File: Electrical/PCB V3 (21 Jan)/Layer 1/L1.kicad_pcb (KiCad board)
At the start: 2 copper layers, 178 x 170 mm, 198 parts, among them J1 Conn_01x02, J3 Conn_01x02, SW1 SW_SPDT, U2 CD74HC4067SM, U3 CD74HC4067SM, U4 XT30UPB-M, U5 113991054

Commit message: finished l1?
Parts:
- J1, J3, TP1: footprint Connector_PinHeader_1.00mm:PinHeader_1x02_P1.00mm_Vertical -> Connector_PinHeader_2.54mm:PinHeader_1x02_P2.54mm_Vertical
- R33, R34: footprint Resistor_SMD:R_0201_0603Metric -> Resistor_SMD:R_0603_1608Metric
- moved U4 245.9 mm to (83.2, 35.6), turned to -45 degrees
- moved U5 196.2 mm to (113.8, 37.8)
- moved SW1 180.9 mm to (89.1, 32.3), turned to 45 degrees
- moved TP1 174.7 mm to (97.7, 37.0), turned to 180 degrees
- moved J3 167.2 mm to (102.2, 36.8), turned to 180 degrees
- moved R33 163.9 mm to (109.0, 29.4), turned to -90 degrees
- moved R34 162.8 mm to (109.1, 33.7), turned to 90 degrees
- moved J1 162.2 mm to (102.2, 43.1), turned to 180 degrees
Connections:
- L10 pad 1: Net-(LED1-A) -> Net-(LED10-A)
- L10 pad 2: Net-(L1-Pad2) -> Net-(L10-Pad2)
- L11 pad 1: Net-(LED1-A) -> Net-(LED11-A)
- L11 pad 2: Net-(L1-Pad2) -> Net-(L11-Pad2)
- L12 pad 1: Net-(LED1-A) -> Net-(LED12-A)
- L12 pad 2: Net-(L1-Pad2) -> Net-(L12-Pad2)
- L13 pad 1: Net-(LED1-A) -> Net-(LED13-A)
- L13 pad 2: Net-(L1-Pad2) -> Net-(L13-Pad2)
- L14 pad 1: Net-(LED1-A) -> Net-(LED14-A)
- L14 pad 2: Net-(L1-Pad2) -> Net-(L14-Pad2)
- L15 pad 1: Net-(LED1-A) -> Net-(LED15-A)
- L15 pad 2: Net-(L1-Pad2) -> Net-(L15-Pad2)
- L16 pad 1: Net-(LED1-A) -> Net-(LED16-A)
- L16 pad 2: Net-(L1-Pad2) -> Net-(L16-Pad2)
- L17 pad 1: Net-(LED1-A) -> Net-(LED17-A)
- L17 pad 2: Net-(L1-Pad2) -> Net-(L17-Pad2)
- L18 pad 1: Net-(LED1-A) -> Net-(LED18-A)
- L18 pad 2: Net-(L1-Pad2) -> Net-(L18-Pad2)
- L19 pad 1: Net-(LED1-A) -> Net-(LED19-A)
- L19 pad 2: Net-(L1-Pad2) -> Net-(L19-Pad2)
- L2 pad 1: Net-(LED1-A) -> Net-(LED2-A)
- L2 pad 2: Net-(L1-Pad2) -> Net-(L2-Pad2)
- L20 pad 1: Net-(LED1-A) -> Net-(LED20-A)
- L20 pad 2: Net-(L1-Pad2) -> Net-(L20-Pad2)
- L21 pad 1: Net-(LED1-A) -> Net-(LED21-A)
- L21 pad 2: Net-(L1-Pad2) -> Net-(L21-Pad2)
- L22 pad 1: Net-(LED1-A) -> Net-(LED22-A)
- L22 pad 2: Net-(L1-Pad2) -> Net-(L22-Pad2)
- L23 pad 1: Net-(LED1-A) -> Net-(LED23-A)
- L23 pad 2: Net-(L1-Pad2) -> Net-(L23-Pad2)
- L24 pad 1: Net-(LED1-A) -> Net-(LED24-A)
- L24 pad 2: Net-(L1-Pad2) -> Net-(L24-Pad2)
- L25 pad 1: Net-(LED1-A) -> Net-(LED25-A)
- L25 pad 2: Net-(L1-Pad2) -> Net-(L25-Pad2)
- L26 pad 1: Net-(LED1-A) -> Net-(LED26-A)
- L26 pad 2: Net-(L1-Pad2) -> Net-(L26-Pad2)
- L27 pad 1: Net-(LED1-A) -> Net-(LED27-A)
- L27 pad 2: Net-(L1-Pad2) -> Net-(L27-Pad2)
- L28 pad 1: Net-(LED1-A) -> Net-(LED28-A)
- L28 pad 2: Net-(L1-Pad2) -> Net-(L28-Pad2)
- L29 pad 1: Net-(LED1-A) -> Net-(LED29-A)
- L29 pad 2: Net-(L1-Pad2) -> Net-(L29-Pad2)
- L3 pad 1: Net-(LED1-A) -> Net-(LED3-A)
- L3 pad 2: Net-(L1-Pad2) -> Net-(L3-Pad2)
- L30 pad 1: Net-(LED1-A) -> Net-(LED30-A)
- L30 pad 2: Net-(L1-Pad2) -> Net-(L30-Pad2)
- L31 pad 1: Net-(LED1-A) -> Net-(LED31-A)
- L31 pad 2: Net-(L1-Pad2) -> Net-(L31-Pad2)
- L32 pad 1: Net-(LED1-A) -> Net-(LED32-A)
- L32 pad 2: Net-(L1-Pad2) -> Net-(L32-Pad2)
- L4 pad 1: Net-(LED1-A) -> Net-(LED4-A)
- L4 pad 2: Net-(L1-Pad2) -> Net-(L4-Pad2)
- L5 pad 1: Net-(LED1-A) -> Net-(LED5-A)
- L5 pad 2: Net-(L1-Pad2) -> Net-(L5-Pad2)
- L6 pad 1: Net-(LED1-A) -> Net-(LED6-A)
- L6 pad 2: Net-(L1-Pad2) -> Net-(L6-Pad2)
- L7 pad 1: Net-(LED1-A) -> Net-(LED7-A)
- L7 pad 2: Net-(L1-Pad2) -> Net-(L7-Pad2)
- L8 pad 1: Net-(LED1-A) -> Net-(LED8-A)
- L8 pad 2: Net-(L1-Pad2) -> Net-(L8-Pad2)
- L9 pad 1: Net-(LED1-A) -> Net-(LED9-A)
- L9 pad 2: Net-(L1-Pad2) -> Net-(L9-Pad2)
- LED10 pad 2: Net-(LED1-A) -> Net-(LED10-A)
- LED11 pad 2: Net-(LED1-A) -> Net-(LED11-A)
- LED12 pad 2: Net-(LED1-A) -> Net-(LED12-A)
- LED13 pad 2: Net-(LED1-A) -> Net-(LED13-A)
- LED14 pad 2: Net-(LED1-A) -> Net-(LED14-A)
- LED15 pad 2: Net-(LED1-A) -> Net-(LED15-A)
- LED16 pad 2: Net-(LED1-A) -> Net-(LED16-A)
- LED17 pad 2: Net-(LED1-A) -> Net-(LED17-A)
- LED18 pad 2: Net-(LED1-A) -> Net-(LED18-A)
- LED19 pad 2: Net-(LED1-A) -> Net-(LED19-A)
- LED2 pad 2: Net-(LED1-A) -> Net-(LED2-A)
- LED20 pad 2: Net-(LED1-A) -> Net-(LED20-A)
- LED21 pad 2: Net-(LED1-A) -> Net-(LED21-A)
- LED22 pad 2: Net-(LED1-A) -> Net-(LED22-A)
- LED23 pad 2: Net-(LED1-A) -> Net-(LED23-A)
- LED24 pad 2: Net-(LED1-A) -> Net-(LED24-A)
- LED25 pad 2: Net-(LED1-A) -> Net-(LED25-A)
- LED26 pad 2: Net-(LED1-A) -> Net-(LED26-A)
- LED27 pad 2: Net-(LED1-A) -> Net-(LED27-A)
- LED28 pad 2: Net-(LED1-A) -> Net-(LED28-A)
- LED29 pad 2: Net-(LED1-A) -> Net-(LED29-A)
- LED3 pad 2: Net-(LED1-A) -> Net-(LED3-A)
- LED30 pad 2: Net-(LED1-A) -> Net-(LED30-A)
- LED31 pad 2: Net-(LED1-A) -> Net-(LED31-A)
- LED32 pad 2: Net-(LED1-A) -> Net-(LED32-A)
- LED4 pad 2: Net-(LED1-A) -> Net-(LED4-A)
- LED5 pad 2: Net-(LED1-A) -> Net-(LED5-A)
- LED6 pad 2: Net-(LED1-A) -> Net-(LED6-A)
- LED7 pad 2: Net-(LED1-A) -> Net-(LED7-A)
- LED8 pad 2: Net-(LED1-A) -> Net-(LED8-A)
- LED9 pad 2: Net-(LED1-A) -> Net-(LED9-A)
- R10 pad 2: Net-(L1-Pad2) -> Net-(L10-Pad2)
- R11 pad 2: Net-(L1-Pad2) -> Net-(L11-Pad2)
- R12 pad 2: Net-(L1-Pad2) -> Net-(L12-Pad2)
- R13 pad 2: Net-(L1-Pad2) -> Net-(L13-Pad2)
- R14 pad 2: Net-(L1-Pad2) -> Net-(L14-Pad2)
- R15 pad 2: Net-(L1-Pad2) -> Net-(L15-Pad2)
- R16 pad 2: Net-(L1-Pad2) -> Net-(L16-Pad2)
- R17 pad 2: Net-(L1-Pad2) -> Net-(L17-Pad2)
- R18 pad 2: Net-(L1-Pad2) -> Net-(L18-Pad2)
- R19 pad 2: Net-(L1-Pad2) -> Net-(L19-Pad2)
- R2 pad 2: Net-(L1-Pad2) -> Net-(L2-Pad2)
- R20 pad 2: Net-(L1-Pad2) -> Net-(L20-Pad2)
- R21 pad 2: Net-(L1-Pad2) -> Net-(L21-Pad2)
- R22 pad 2: Net-(L1-Pad2) -> Net-(L22-Pad2)
- R23 pad 2: Net-(L1-Pad2) -> Net-(L23-Pad2)
- R24 pad 2: Net-(L1-Pad2) -> Net-(L24-Pad2)
- R25 pad 2: Net-(L1-Pad2) -> Net-(L25-Pad2)
- R26 pad 2: Net-(L1-Pad2) -> Net-(L26-Pad2)
- R27 pad 2: Net-(L1-Pad2) -> Net-(L27-Pad2)
- R28 pad 2: Net-(L1-Pad2) -> Net-(L28-Pad2)
- R29 pad 2: Net-(L1-Pad2) -> Net-(L29-Pad2)
- R3 pad 2: Net-(L1-Pad2) -> Net-(L3-Pad2)
- R30 pad 2: Net-(L1-Pad2) -> Net-(L30-Pad2)
- R31 pad 2: Net-(L1-Pad2) -> Net-(L31-Pad2)
- R32 pad 2: Net-(L1-Pad2) -> Net-(L32-Pad2)
- R33 pad 2: /Mux Com (1-16) -> /Mux Com (17-32)
- R34 pad 2: /Mux Com (17-32) -> /Mux Com (1-16)
- R4 pad 2: Net-(L1-Pad2) -> Net-(L4-Pad2)
- R5 pad 2: Net-(L1-Pad2) -> Net-(L5-Pad2)
- R6 pad 2: Net-(L1-Pad2) -> Net-(L6-Pad2)
- R7 pad 2: Net-(L1-Pad2) -> Net-(L7-Pad2)
- R8 pad 2: Net-(L1-Pad2) -> Net-(L8-Pad2)
- R9 pad 2: Net-(L1-Pad2) -> Net-(L9-Pad2)
- U2 pad 1: /Mux Com (1-16) -> /Mux Com (17-32)
- U3 pad 1: /Mux Com (17-32) -> /Mux Com (1-16)
- U5 pad 1: /Mux Com (1-16) -> /Mux Com (17-32)
- U5 pad 2: /Mux Com (17-32) -> /Mux Com (1-16)
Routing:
- net +3V3: track 0.00 -> 142.5 mm
- net /Mux Com (17-32): track 0.00 -> 95.9 mm, vias 0 -> 1
- net /Mux Com (1-16): track 0.00 -> 92.1 mm, vias 0 -> 1
- net /S0: track 0.00 -> 89.8 mm, vias 0 -> 3
- net /S2: track 0.00 -> 84.4 mm, vias 0 -> 3
- net /S1: track 0.00 -> 84.2 mm, vias 0 -> 3
- net /S3: track 0.00 -> 79.3 mm, vias 0 -> 3
- net Net-(LED1-A): track 72.5 -> 2.27 mm
- net Net-(L1-Pad2): track 61.2 -> 1.91 mm
- net Net-(U2-I5): track 0.00 -> 57.1 mm
- net Net-(U2-I4): track 0.00 -> 55.5 mm
- net Net-(U2-I3): track 0.00 -> 54.8 mm
- net Net-(U2-I0): track 0.00 -> 50.8 mm
- net Net-(U2-I12): track 0.00 -> 50.6 mm
- net Net-(U2-I6): track 0.00 -> 50.3 mm
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
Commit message: finished layer1?
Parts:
- added C33: C, Capacitor_SMD:C_0603_1608Metric, B.Cu at (98.8, 111.3)
- added C34: C, Capacitor_SMD:C_0603_1608Metric, B.Cu at (128.8, 104.3)
- moved L24 3.00 mm to (160.2, 117.0)
- moved LED16 3.00 mm to (103.9, 157.3)
- moved LED32 3.00 mm to (123.6, 58.3)
- moved LED8 3.00 mm to (64.2, 97.9)
- moved L32 3.00 mm to (123.0, 61.4)
- moved L8 3.00 mm to (67.4, 98.6)
- moved L16 3.00 mm to (104.5, 154.2)
- moved LED24 3.00 mm to (163.3, 117.6)
- moved L23 3.00 mm to (157.5, 125.9)
- moved L27 3.00 mm to (157.5, 89.7)
- moved LED11 3.00 mm to (67.1, 127.1)
- moved LED7 3.00 mm to (67.1, 88.5)
- moved L3 3.00 mm to (95.7, 64.1)
- moved LED3 3.00 mm to (94.4, 61.1)
- moved LED31 3.00 mm to (133.1, 61.1)
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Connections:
- U2 pad 24: +3V3 -> Net-(U2-VCC)
- U3 pad 24: +3V3 -> Net-(U3-VCC)
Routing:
- net Net-(U2-I11): track 46.7 -> 0.00 mm
- net Net-(U3-I4): track 46.7 -> 89.3 mm
- net +3V3: track 142.5 -> 131.5 mm
- net Net-(U3-I9): track 50.3 -> 45.5 mm
- net Net-(U2-I6): track 50.3 -> 45.5 mm
- net Net-(U2-VCC): track 0.00 -> 3.76 mm
- net Net-(U3-VCC): track 0.00 -> 3.75 mm
- net Net-(U3-I3): track 50.6 -> 46.9 mm
- net Net-(U2-I12): track 50.6 -> 46.9 mm
- net Net-(L15-Pad2): track 1.91 -> 5.03 mm
- net Net-(L7-Pad2): track 1.91 -> 5.03 mm
- net Net-(L23-Pad2): track 1.91 -> 5.03 mm
- net Net-(L31-Pad2): track 1.91 -> 5.03 mm
- net Net-(L16-Pad2): track 1.91 -> 5.03 mm
- net Net-(L24-Pad2): track 1.91 -> 5.03 mm
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
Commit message: added l3 v3 dxf, did somemore l1
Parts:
- removed J3: Conn_01x02, Connector_PinHeader_2.54mm:PinHeader_1x02_P2.54mm_Vertical
- removed SW1: SW_SPDT, Button_Switch_SMD:Nidec_Copal_CAS-120A
- removed U4: XT30UPB-M, Connector_AMASS:AMASS_XT30U-M_1x02_P5.0mm_Vertical
- J1: value Conn_01x02 -> Conn_01x04; footprint Connector_PinHeader_2.54mm:PinHeader_1x02_P2.54mm_Vertical -> Connector_JST:JST_EH_B4B-EH-A_1x04_P2.50mm_Vertical
- moved TP1 14.0 mm to (83.8, 37.8)
- moved J1 8.44 mm to (93.8, 42.8), turned to 90 degrees
- moved C33 2.00 mm to (100.8, 111.3)
- moved C34 2.00 mm to (126.8, 104.3)
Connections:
- J1 pad 1: /UART (TX) -> GND
- J1 pad 2: /UART (RX) -> /L1 TX
- U5 pad 5: /SDA -> unconnected-(U5-D4-Pad5)
- U5 pad 6: /SCL -> unconnected-(U5-D5-Pad6)
- U5 pad 7: /UART (TX) -> /L1 TX
- U5 pad 8: /UART (RX) -> /L1 RX
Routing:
- net Net-(U3-I4): track 89.3 -> 44.7 mm
- net Net-(U2-I11): track 0.00 -> 44.7 mm
- net /L1 RX: track 0.00 -> 30.8 mm
- net +3V3: track 131.5 -> 157.3 mm
- net /UART (RX): track 21.2 -> 0.00 mm
- net /L1 TX: track 0.00 -> 14.5 mm
- net /SCL: track 7.77 -> 0.00 mm
- net /SDA: track 7.77 -> 0.00 mm
- net Net-(SW1-A): track 5.44 -> 0.00 mm
- net /UART (TX): track 4.94 -> 0.00 mm
- net Net-(U3-VCC): track 3.75 -> 1.75 mm
- net Net-(U2-VCC): track 3.76 -> 1.76 mm
- net Net-(L29-Pad2): track 5.03 -> 4.43 mm
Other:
- board text added: "2-Chairs."
- board text added: "no"

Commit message: did somemore l1
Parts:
- moved C33 0.78 mm to (100.8, 110.5), turned to -90 degrees
- moved C34 0.78 mm to (126.8, 105.1), turned to 90 degrees
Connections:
- C33 pad 1: +3V3 -> GND
- C33 pad 2: Net-(U3-VCC) -> +3V3
- C34 pad 1: +3V3 -> GND
- C34 pad 2: Net-(U2-VCC) -> +3V3
- U2 pad 24: Net-(U2-VCC) -> +3V3
- U3 pad 24: Net-(U3-VCC) -> +3V3
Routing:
- net +3V3: track 157.3 -> 163.9 mm
- net Net-(U2-VCC): track 1.76 -> 0.00 mm
- net Net-(U3-VCC): track 1.75 -> 0.00 mm
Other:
- board text added: "{dblquote}looks decent lah{dblquote} -yuzhe"
- board text removed: "no"

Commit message: almost done with l1? more vetting done
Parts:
- moved R34 1.27 mm to (107.8, 33.6)
- moved R33 1.18 mm to (107.8, 29.4)
- moved C33 1.00 mm to (101.8, 110.5)
- moved C34 1.00 mm to (125.8, 105.1)

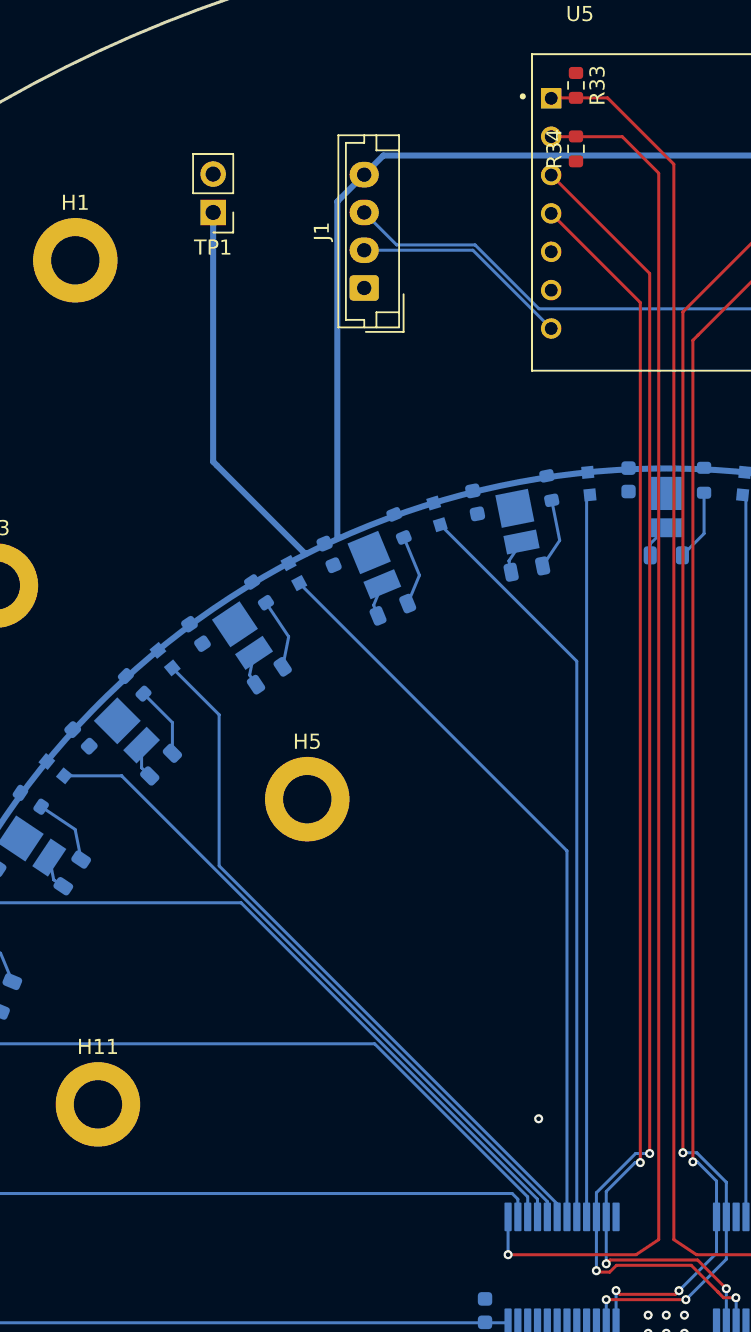
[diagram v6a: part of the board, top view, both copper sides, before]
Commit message: uploaded print files, added credits to l1
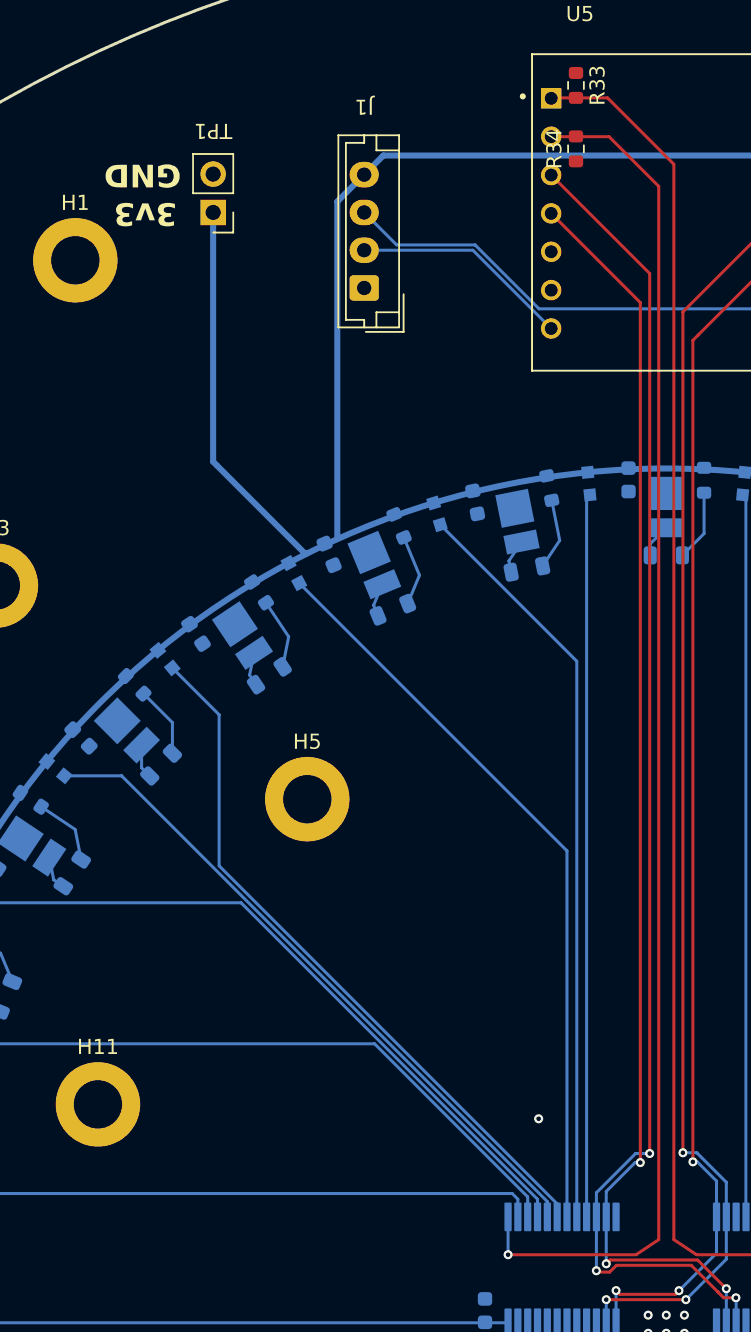
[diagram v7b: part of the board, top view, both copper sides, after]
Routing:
- net /Mux Com (1-16): track 91.5 -> 91.0 mm
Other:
- board text added: "3v3"
- board text added: "GND"
- board text added: "In the grand tapestry of our design endeavor, we owe a debt of profound gratitude to the esteemed teams of Sentinels Robotics, ducc. & Dynamo, whose brilliant schematics and designs have guided our efforts."
- board text added: "{dblquote}looks decent lah{dblquote} -yuzhe (not an elec guy)"
- board text removed: "{dblquote}looks decent lah{dblquote} -yuzhe"
